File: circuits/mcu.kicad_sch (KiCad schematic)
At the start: 35 parts, among them J1 USB_MINI_B, J2 USB_MINI_B, Q5 Q_L8050QLT1G, Q6 Q_L8550HQLT1G, SW1 SW_PUSH, SW2 SW_PUSH, SW3 SW_PUSH, U10 CP2102N-Axx-xQFN28, U9 ESP32-S3-WROOM-1

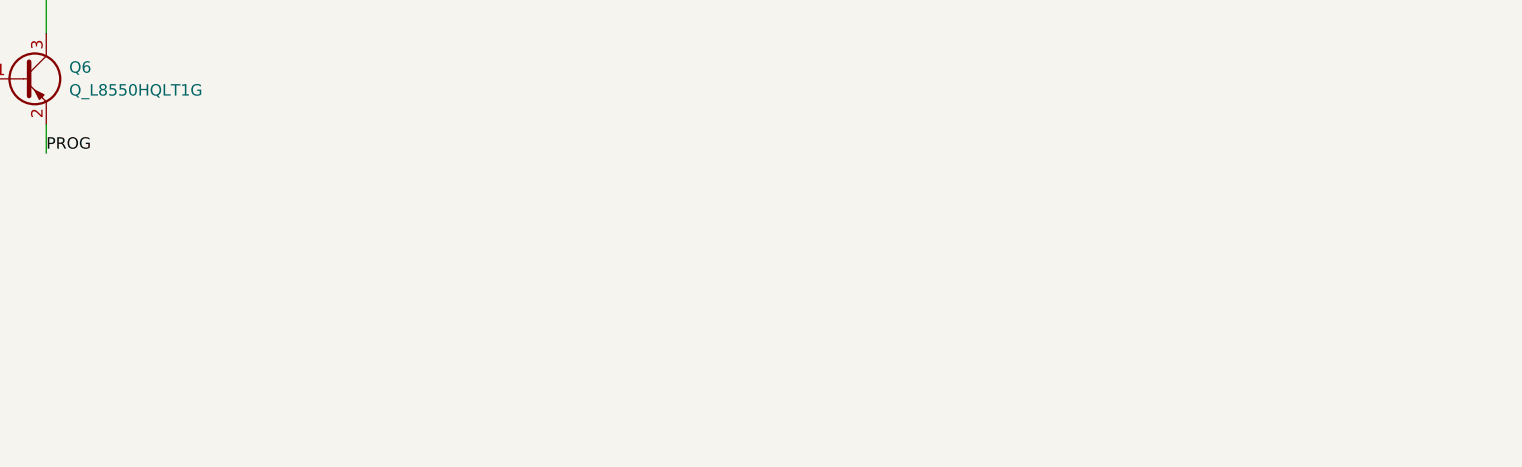
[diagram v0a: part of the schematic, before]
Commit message: Label laser controller board sections
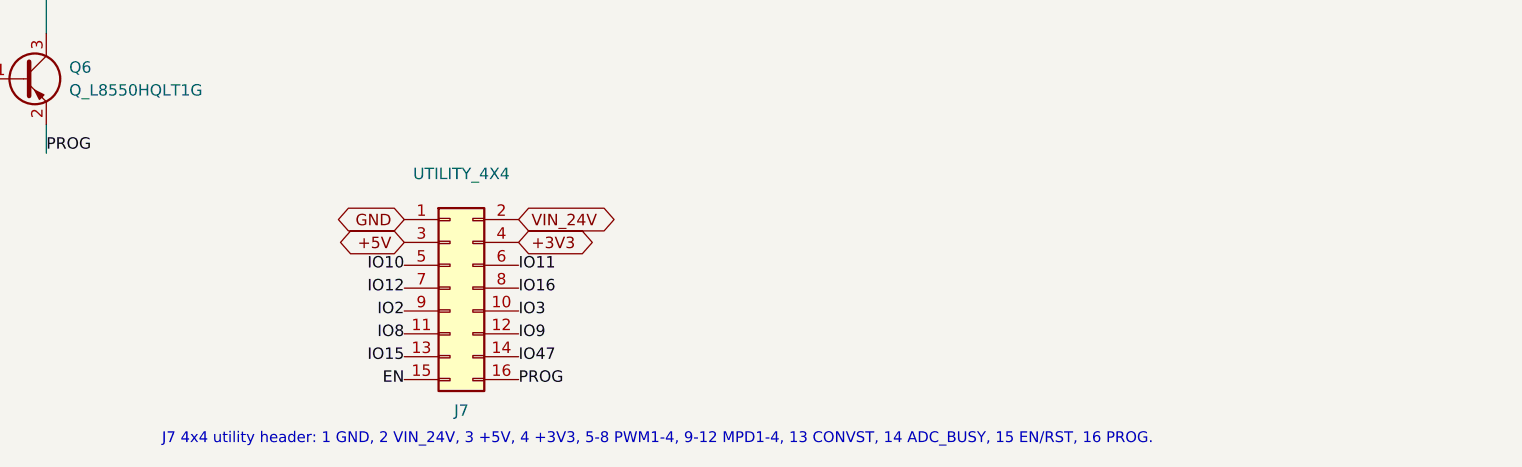
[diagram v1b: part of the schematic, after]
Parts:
- added J7: UTILITY_4X4, Open_Automation:PinHeader_4x04_P2.54mm_Vertical, symbol Open_Automation:Conn_04x04_Utility
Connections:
- net EN: now also J7.15 (Pin_15)
- net GND: now also J7.1 (Pin_1)
- net IO10: now also J7.5 (Pin_5)
- net IO11: now also J7.6 (Pin_6)
- net IO12: now also J7.7 (Pin_7)
- net IO15: now also J7.13 (Pin_13)
- net IO16: now also J7.8 (Pin_8)
- net IO2: now also J7.9 (Pin_9)
- net IO3: now also J7.10 (Pin_10)
- net IO47: now also J7.14 (Pin_14)
- net IO8: now also J7.11 (Pin_11)
- net IO9: now also J7.12 (Pin_12)
- net PROG: now also J7.16 (Pin_16)
- new net +3V3: J7.4 (Pin_4)
- new net +5V: J7.3 (Pin_3)
- new net VIN_24V: J7.2 (Pin_2)
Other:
- note added: "J7 4x4 utility header: 1 GND, 2 VIN_24V, 3 +5V, 4 +3V3, 5-8 PWM1-4, 9-12 MPD1-4, 13 CONVST, 14 ADC_BUSY, 15 EN/RST, 16 PROG."
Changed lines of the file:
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@@
+    )
+  )
+  (global_label "GND" (shape bidirectional) (at 359.92 212.38 180)
+    (effects (font (size 1.27 1.27)) (justify right))
+  )
+  (global_label "VIN_24V" (shape bidirectional) (at 372.62 212.38 0)
+    (effects (font (size 1.27 1.27)) (justify left))
+  )
+  (global_label "+5V" (shape bidirectional) (at 359.92 214.92 180)
+    (effects (font (size 1.27 1.27)) (justify right))
+  )
+  (global_label "+3V3" (shape bidirectional) (at 372.62 214.92 0)
+    (effects (font (size 1.27 1.27)) (justify left))
+  )
+  (label "IO10" (at 359.92 217.46 180)
+    (effects (font (size 1.27 1.27)) (justify right))
+  )
+  (label "IO11" (at 372.62 217.46 0)
+    (effects (font (size 1.27 1.27)) (justify left))
+  )
+  (label "IO12" (at 359.92 220 180)
+    (effects (font (size 1.27 1.27)) (justify right))
+  )
+  (label "IO16" (at 372.62 220 0)
+    (effects (font (size 1.27 1.27)) (justify left))
+  )
+  (label "IO2" (at 359.92 222.54 180)
+    (effects (font (size 1.27 1.27)) (justify right))
+  )
+  (label "IO3" (at 372.62 222.54 0)
+    (effects (font (size 1.27 1.27)) (justify left))
+  )
+  (label "IO8" (at 359.92 225.08 180)
+    (effects (font (size 1.27 1.27)) (justify right))
+  )
+  (label "IO9" (at 372.62 225.08 0)
+    (effects (font (size 1.27 1.27)) (justify left))
+  )
+  (label "IO15" (at 359.92 227.62 180)
+    (effects (font (size 1.27 1.27)) (justify right))
+  )
+  (label "IO47" (at 372.62 227.62 0)
+    (effects (font (size 1.27 1.27)) (justify left))
+  )
+  (label "EN" (at 359.92 230.16 180)
+    (effects (font (size 1.27 1.27)) (justify right))
+  )
+  (label "PROG" (at 372.62 230.16 0)
+    (effects (font (size 1.27 1.27)) (justify left))
+  )
+  (text "J7 4x4 utility header: 1 GND, 2 VIN_24V, 3 +5V, 4 +3V3, 5-8 PWM1-4, 9-12 MPD1-4, 13 CONVST, 14 ADC_BUSY, 15 EN/RST, 16 PROG."
+    (at 333 236.8 0)
+    (effects (font (size 1.2 1.2)) (justify left))
+  )
+  (symbol (lib_id "Open_Automation:Conn_04x04_Utility") (at 365 220 0) (unit 1)
+    (in_bom yes) (on_board yes) (dnp no)
+    (property "Reference" "J7" (at 366.27 233.6 0)
+      (effects (font (size 1.27 1.27)))
+    )
+    (property "Value" "UTILITY_4X4" (at 366.27 207.3 0)
+      (effects (font (size 1.27 1.27)))
+    )
+    (property "Footprint" "Open_Automation:PinHeader_4x04_P2.54mm_Vertical" (at 365 220 0)
+      (effects (font (size 1.27 1.27)) hide)
+    )
+    (property "Datasheet" "~" (at 365 220 0)
+      (effects (font (size 1.27 1.27)) hide)
+    )
+    (pin "1")
+    (pin "2")
+    (pin "3")
+    (pin "4")
+    (pin "5")
+    (pin "6")
+    (pin "7")
+    (pin "8")
+    (pin "9")
+    (pin "10")
+    (pin "11")
+    (pin "12")
+    (pin "13")
+    (pin "14")
+    (pin "15")
+    (pin "16")
+    (instances
+      (project "laser_controller"
+        (path "/c1d2e3f4-6000-4000-a000-000000000001/c1d2e3f4-6000-4000-a000-000000001543"
+          (reference "J7") (unit 1)
+        )
+      )
     )
   )

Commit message: Use SMT 4x2 utility header
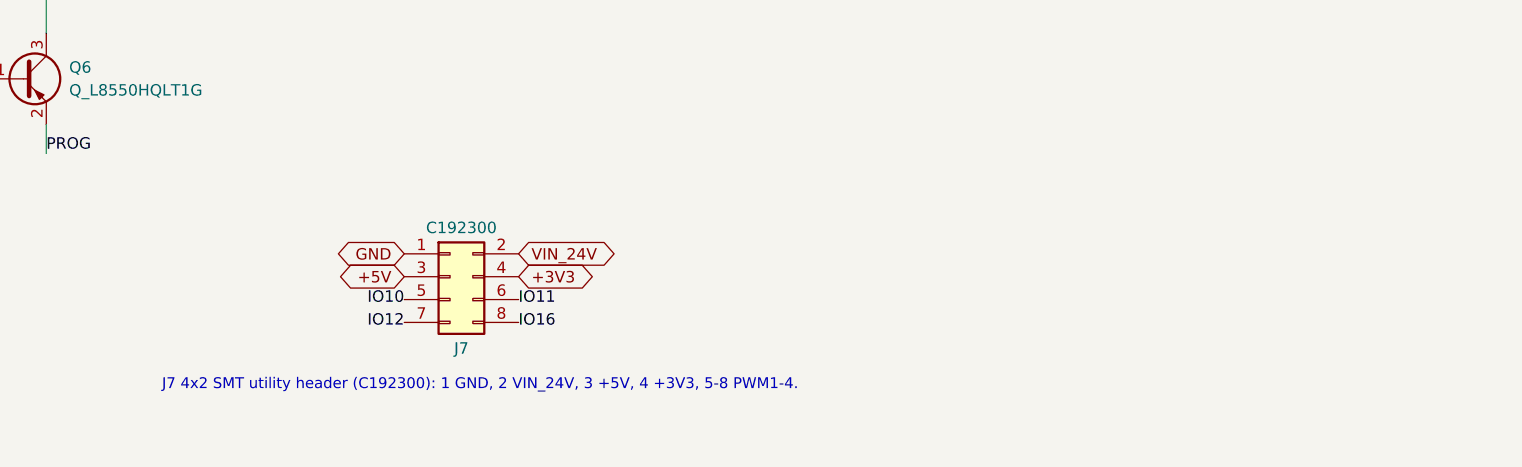
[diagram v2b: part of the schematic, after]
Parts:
- J7: value UTILITY_4X4 -> C192300; footprint Open_Automation:PinHeader_4x04_P2.54mm_Vertical -> Open_Automation:PinHeader_2x04_P2.54mm_SMD_Vertical_C192300; symbol Open_Automation:Conn_04x04_Utility -> Open_Automation:Conn_02x04_Utility_C192300; LCSC (none) -> C192300; Manufacturer (none) -> BOOMELE(Boom Precision Elec); Part Number (none) -> 2.54-2*4P
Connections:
- net EN: no longer J7.15 (Pin_15)
- net IO15: no longer J7.13 (Pin_13)
- net IO2: no longer J7.9 (Pin_9)
- net IO3: no longer J7.10 (Pin_10)
- net IO47: no longer J7.14 (Pin_14)
- net IO8: no longer J7.11 (Pin_11)
- net IO9: no longer J7.12 (Pin_12)
- net PROG: no longer J7.16 (Pin_16)
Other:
- note added: "J7 4x2 SMT utility header (C192300): 1 GND, 2 VIN_24V, 3 +5V, 4 +3V3, 5-8 PWM1-4."
- note removed: "J7 4x4 utility header: 1 GND, 2 VIN_24V, 3 +5V, 4 +3V3, 5-8 PWM1-4, 9-12 MPD1-4, 13 CONVST, 14 ADC_BUSY, 15 EN/RST, 16 PROG."
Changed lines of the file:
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@@
     )
   )
-  (global_label "GND" (shape bidirectional) (at 359.92 212.38 180)
+  (global_label "GND" (shape bidirectional) (at 359.92 216.19 180)
     (effects (font (size 1.27 1.27)) (justify right))
   )
-  (global_label "VIN_24V" (shape bidirectional) (at 372.62 212.38 0)
+  (global_label "VIN_24V" (shape bidirectional) (at 372.62 216.19 0)
     (effects (font (size 1.27 1.27)) (justify left))
   )
-  (global_label "+5V" (shape bidirectional) (at 359.92 214.92 180)
+  (global_label "+5V" (shape bidirectional) (at 359.92 218.73 180)
     (effects (font (size 1.27 1.27)) (justify right))
   )
-  (global_label "+3V3" (shape bidirectional) (at 372.62 214.92 0)
+  (global_label "+3V3" (shape bidirectional) (at 372.62 218.73 0)
     (effects (font (size 1.27 1.27)) (justify left))
   )
-  (label "IO10" (at 359.92 217.46 180)
+  (label "IO10" (at 359.92 221.27 180)
     (effects (font (size 1.27 1.27)) (justify right))
   )
-  (label "IO11" (at 372.62 217.46 0)
+  (label "IO11" (at 372.62 221.27 0)
     (effects (font (size 1.27 1.27)) (justify left))
   )
-  (label "IO12" (at 359.92 220 180)
+  (label "IO12" (at 359.92 223.81 180)
     (effects (font (size 1.27 1.27)) (justify right))
   )
-  (label "IO16" (at 372.62 220 0)
+  (label "IO16" (at 372.62 223.81 0)
     (effects (font (size 1.27 1.27)) (justify left))
   )
-  (label "IO2" (at 359.92 222.54 180)
-    (effects (font (size 1.27 1.27)) (justify right))
-  )
-  (label "IO3" (at 372.62 222.54 0)
-    (effects (font (size 1.27 1.27)) (justify left))
-  )
-  (label "IO8" (at 359.92 225.08 180)
-    (effects (font (size 1.27 1.27)) (justify right))
-  )
-  (label "IO9" (at 372.62 225.08 0)
-    (effects (font (size 1.27 1.27)) (justify left))
-  )
-  (label "IO15" (at 359.92 227.62 180)
-    (effects (font (size 1.27 1.27)) (justify right))
-  )
-  (label "IO47" (at 372.62 227.62 0)
-    (effects (font (size 1.27 1.27)) (justify left))
-  )
-  (label "EN" (at 359.92 230.16 180)
-    (effects (font (size 1.27 1.27)) (justify right))
-  )
-  (label "PROG" (at 372.62 230.16 0)
-    (effects (font (size 1.27 1.27)) (justify left))
-  )
-  (text "J7 4x4 utility header: 1 GND, 2 VIN_24V, 3 +5V, 4 +3V3, 5-8 PWM1-4, 9-12 MPD1-4, 13 CONVST, 14 ADC_BUSY, 15 EN/RST, 16 PROG."
-    (at 333 236.8 0)
+  (text "J7 4x2 SMT utility header (C192300): 1 GND, 2 VIN_24V, 3 +5V, 4 +3V3, 5-8 PWM1-4."
+    (at 333 230.8 0)
     (effects (font (size 1.2 1.2)) (justify left))
   )
-  (symbol (lib_id "Open_Automation:Conn_04x04_Utility") (at 365 220 0) (unit 1)
+  (symbol (lib_id "Open_Automation:Conn_02x04_Utility_C192300") (at 365 220 0) (unit 1)
     (in_bom yes) (on_board yes) (dnp no)
-    (property "Reference" "J7" (at 366.27 233.6 0)
+    (property "Reference" "J7" (at 366.27 226.7 0)
       (effects (font (size 1.27 1.27)))
     )
-    (property "Value" "UTILITY_4X4" (at 366.27 207.3 0)
+    (property "Value" "C192300" (at 366.27 213.3 0)
       (effects (font (size 1.27 1.27)))
     )
-    (property "Footprint" "Open_Automation:PinHeader_4x04_P2.54mm_Vertical" (at 365 220 0)
+    (property "Footprint" "Open_Automation:PinHeader_2x04_P2.54mm_SMD_Vertical_C192300" (at 365 220 0)
       (effects (font (size 1.27 1.27)) hide)
     )
-    (property "Datasheet" "~" (at 365 220 0)
+    (property "Datasheet" "https://www.lcsc.com/product-detail/C192300.html" (at 365 220 0)
+      (effects (font (size 1.27 1.27)) hide)
+    )
+    (property "Manufacturer" "BOOMELE(Boom Precision Elec)" (at 365 220 0)
+      (effects (font (size 1.27 1.27)) hide)
+    )
+    (property "Part Number" "2.54-2*4P" (at 365 220 0)
+      (effects (font (size 1.27 1.27)) hide)
+    )
+    (property "LCSC" "C192300" (at 365 220 0)
       (effects (font (size 1.27 1.27)) hide)
     )
@@
     (pin "7")
     (pin "8")
-    (pin "9")
-    (pin "10")
-    (pin "11")
-    (pin "12")
-    (pin "13")
-    (pin "14")
-    (pin "15")
-    (pin "16")
     (instances
       (project "laser_controller"

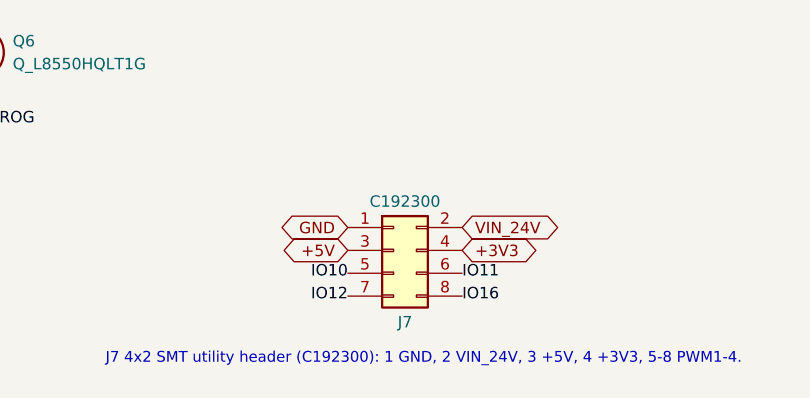
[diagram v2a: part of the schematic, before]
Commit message: Clarify 4x2 utility header signals
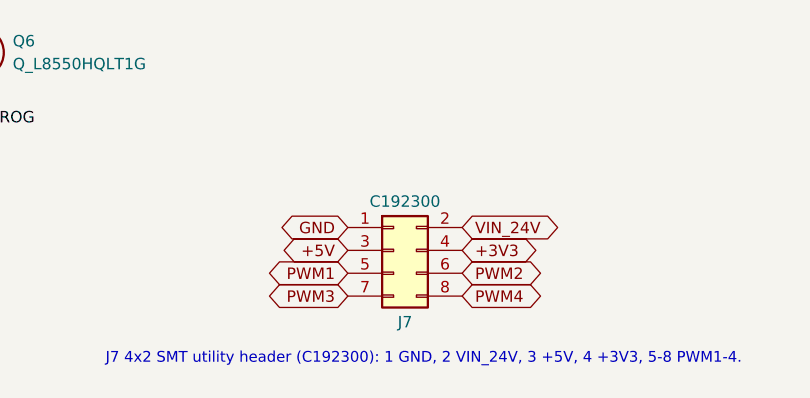
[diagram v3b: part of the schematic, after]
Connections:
- net IO10: no longer J7.5 (Pin_5)
- net IO11: no longer J7.6 (Pin_6)
- net IO12: no longer J7.7 (Pin_7)
- net IO16: no longer J7.8 (Pin_8)
- new net PWM1: J7.5 (PWM1)
- new net PWM2: J7.6 (PWM2)
- new net PWM3: J7.7 (PWM3)
- new net PWM4: J7.8 (PWM4)
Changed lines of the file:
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@@
     (effects (font (size 1.27 1.27)) (justify left))
   )
-  (label "IO10" (at 359.92 221.27 180)
+  (global_label "PWM1" (shape bidirectional) (at 359.92 221.27 180)
     (effects (font (size 1.27 1.27)) (justify right))
   )
-  (label "IO11" (at 372.62 221.27 0)
+  (global_label "PWM2" (shape bidirectional) (at 372.62 221.27 0)
     (effects (font (size 1.27 1.27)) (justify left))
   )
-  (label "IO12" (at 359.92 223.81 180)
+  (global_label "PWM3" (shape bidirectional) (at 359.92 223.81 180)
     (effects (font (size 1.27 1.27)) (justify right))
   )
-  (label "IO16" (at 372.62 223.81 0)
+  (global_label "PWM4" (shape bidirectional) (at 372.62 223.81 0)
     (effects (font (size 1.27 1.27)) (justify left))
   )

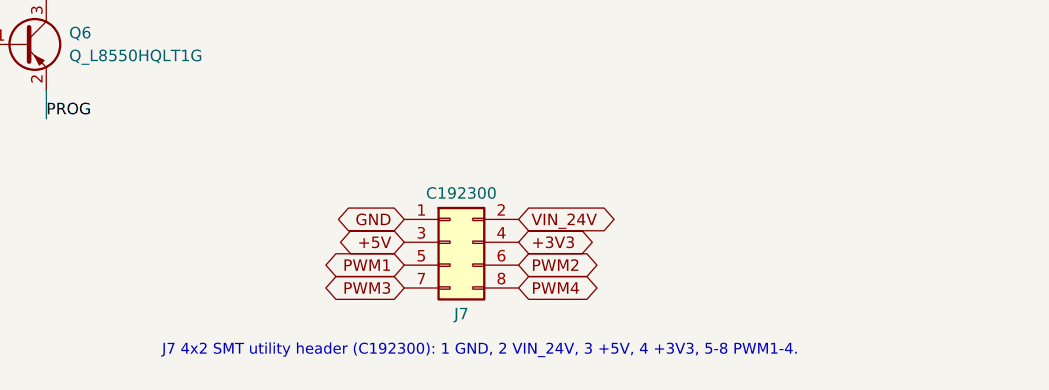
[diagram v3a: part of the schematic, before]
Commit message: Mirror power rails on 4x2 header
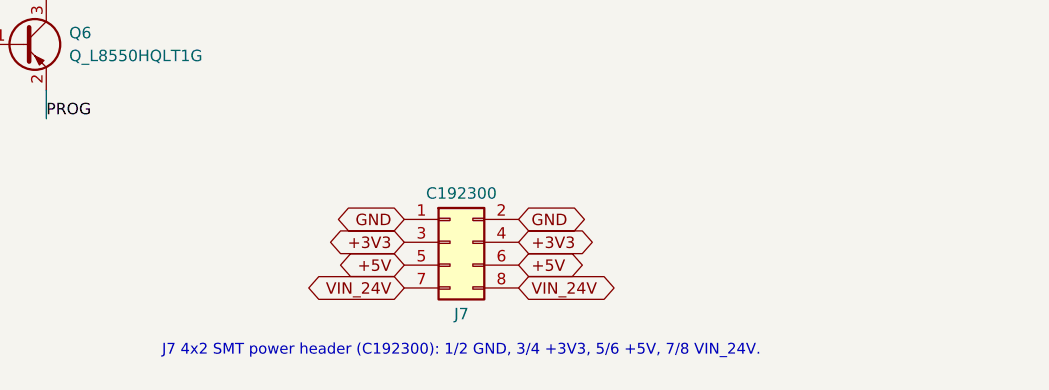
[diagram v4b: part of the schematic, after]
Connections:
- net PWM1 is gone; now on net +5V: J7.5 (+5V)
- net PWM2 is gone; now on net +5V: J7.6 (+5V)
- net PWM3 is gone; now on net VIN_24V: J7.7 (VIN_24V)
- net PWM4 is gone; now on net VIN_24V: J7.8 (VIN_24V)
- net +3V3: now also J7.3 (+3V3)
- net +5V: no longer J7.3 (+5V)
- net GND: now also J7.2 (GND)
- net VIN_24V: no longer J7.2 (VIN_24V)
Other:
- note added: "J7 4x2 SMT power header (C192300): 1/2 GND, 3/4 +3V3, 5/6 +5V, 7/8 VIN_24V."
- note removed: "J7 4x2 SMT utility header (C192300): 1 GND, 2 VIN_24V, 3 +5V, 4 +3V3, 5-8 PWM1-4."
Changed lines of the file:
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@@
     (effects (font (size 1.27 1.27)) (justify right))
   )
-  (global_label "VIN_24V" (shape bidirectional) (at 372.62 216.19 0)
+  (global_label "GND" (shape bidirectional) (at 372.62 216.19 0)
     (effects (font (size 1.27 1.27)) (justify left))
   )
-  (global_label "+5V" (shape bidirectional) (at 359.92 218.73 180)
+  (global_label "+3V3" (shape bidirectional) (at 359.92 218.73 180)
     (effects (font (size 1.27 1.27)) (justify right))
   )
@@
     (effects (font (size 1.27 1.27)) (justify left))
   )
-  (global_label "PWM1" (shape bidirectional) (at 359.92 221.27 180)
+  (global_label "+5V" (shape bidirectional) (at 359.92 221.27 180)
     (effects (font (size 1.27 1.27)) (justify right))
   )
-  (global_label "PWM2" (shape bidirectional) (at 372.62 221.27 0)
+  (global_label "+5V" (shape bidirectional) (at 372.62 221.27 0)
     (effects (font (size 1.27 1.27)) (justify left))
   )
-  (global_label "PWM3" (shape bidirectional) (at 359.92 223.81 180)
+  (global_label "VIN_24V" (shape bidirectional) (at 359.92 223.81 180)
     (effects (font (size 1.27 1.27)) (justify right))
   )
-  (global_label "PWM4" (shape bidirectional) (at 372.62 223.81 0)
+  (global_label "VIN_24V" (shape bidirectional) (at 372.62 223.81 0)
     (effects (font (size 1.27 1.27)) (justify left))
   )
-  (text "J7 4x2 SMT utility header (C192300): 1 GND, 2 VIN_24V, 3 +5V, 4 +3V3, 5-8 PWM1-4."
+  (text "J7 4x2 SMT power header (C192300): 1/2 GND, 3/4 +3V3, 5/6 +5V, 7/8 VIN_24V."
     (at 333 230.8 0)
     (effects (font (size 1.2 1.2)) (justify left))
